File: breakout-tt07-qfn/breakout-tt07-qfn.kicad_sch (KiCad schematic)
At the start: 42 parts, among them J1 Conn_01x04, U1 Openframe_QFN_TT06_REV2, U2 24LC02

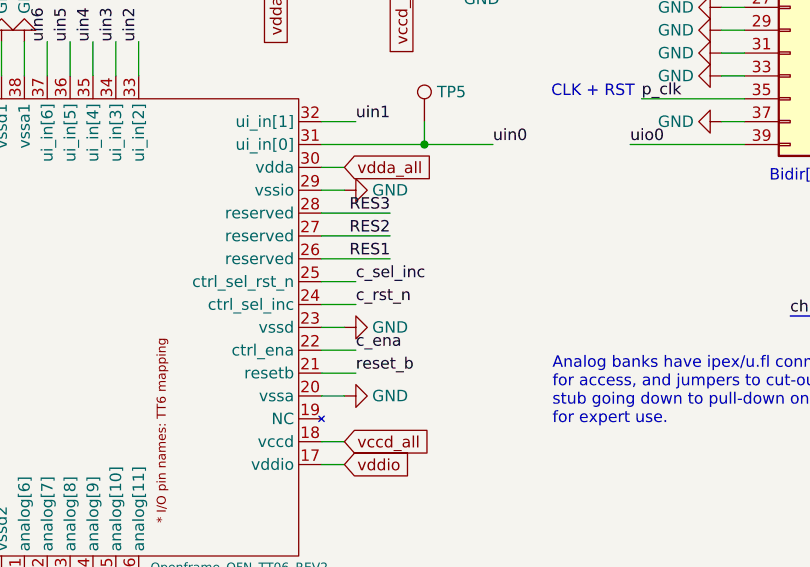
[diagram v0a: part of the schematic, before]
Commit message: fix for mystery regression on MUX rst/sel lines
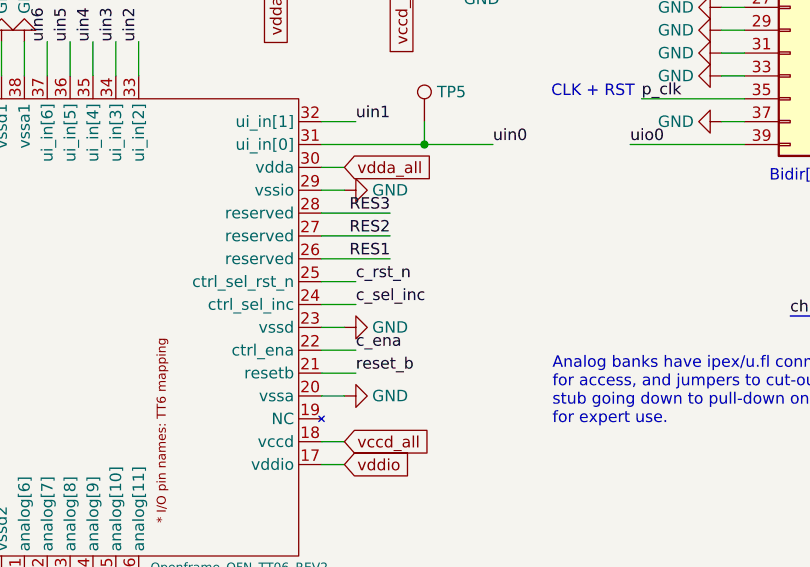
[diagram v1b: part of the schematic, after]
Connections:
- net c_rst_n: now also U1.25 (ctrl_sel_rst_n); no longer U1.24 (ctrl_sel_inc)
- net c_sel_inc: now also U1.24 (ctrl_sel_inc); no longer U1.25 (ctrl_sel_rst_n)
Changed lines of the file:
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@@
 	)
 	(label "c_sel_inc"
-		(at 130.81 91.44 0)
+		(at 130.81 93.98 0)
 		(fields_autoplaced yes)
 		(effects
@@
 	)
 	(label "c_rst_n"
-		(at 130.81 93.98 0)
-		(fields_autoplaced yes)
-		(effects
+		(at 130.81 91.44 0)
+		(fields_autoplaced yes)
+		(effects
